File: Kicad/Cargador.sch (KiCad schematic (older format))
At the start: 7 parts, among them P3 USB_A, U4 MCP73831

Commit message: Agregados footprints de pin headers para elementos faltantes (falta USB)
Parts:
- D1: footprint (none) -> EMG:Pin_Header_Straight_1x02_Pitch2.54mm
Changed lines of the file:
@@
 F 0 "D1" H 4150 3450 50  0000 C CNN
 F 1 "LED" H 4150 3250 50  0000 C CNN
-F 2 "" H 4150 3350 50  0001 C CNN
+F 2 "EMG:Pin_Header_Straight_1x02_Pitch2.54mm" H 4150 3350 50  0001 C CNN
 F 3 "" H 4150 3350 50  0000 C CNN
 	1    4150 3350
@@
 	5700 3250 6000 3250
 $Comp
-L +BATT #PWR25
+L +BATT #PWR023
 U 1 1 57E062FB
 P 6400 3100
-F 0 "#PWR25" H 6400 2950 50  0001 C CNN
+F 0 "#PWR023" H 6400 2950 50  0001 C CNN
 F 1 "+BATT" H 6400 3240 50  0000 C CNN
 F 2 "" H 6400 3100 50  0000 C CNN
@@
 Connection ~ 3900 3100
 $Comp
-L GND #PWR23
+L GND #PWR024
 U 1 1 57FAD4CF
 P 3900 3400
-F 0 "#PWR23" H 3900 3150 50  0001 C CNN
+F 0 "#PWR024" H 3900 3150 50  0001 C CNN
 F 1 "GND" H 3900 3250 50  0000 C CNN
 F 2 "" H 3900 3400 50  0000 C CNN
@@
 $EndComp
 $Comp
-L GND #PWR24
+L GND #PWR025
 U 1 1 57FAD4F1
 P 6000 3550
-F 0 "#PWR24" H 6000 3300 50  0001 C CNN
+F 0 "#PWR025" H 6000 3300 50  0001 C CNN
 F 1 "GND" H 6000 3400 50  0000 C CNN
 F 2 "" H 6000 3550 50  0000 C CNN

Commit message: Footprint del conector micro-usb vertical realizado.
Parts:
- P3: footprint (none) -> EMG:usb_vert
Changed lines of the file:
@@
 F 0 "P3" H 3300 3100 50  0000 C CNN
 F 1 "USB_A" H 3050 3500 50  0000 C CNN
-F 2 "" V 3050 3200 50  0001 C CNN
+F 2 "EMG:usb_vert" V 3050 3200 50  0001 C CNN
 F 3 "" V 3050 3200 50  0000 C CNN
 	1    3100 3300

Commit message: Se inició con el Pcb. Se eliminó el capacitor del socket del nrf. Se cambió el conector de la bat.
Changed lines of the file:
@@
 	4300 3550 4150 3550
 Wire Wire Line
-	4150 3150 4150 3100
+	4150 3100 4150 3150
 Wire Wire Line
 	3400 3100 4750 3100

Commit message: Versión unificada
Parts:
- C7, C8: footprint EMG:C_0805 -> EMG:C_0603
- R21, R22: footprint EMG:R_0805 -> EMG:R_0603
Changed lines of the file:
@@
 F 0 "C8" H 6425 3450 50  0000 L CNN
 F 1 "CP" H 6425 3250 50  0000 L CNN
-F 2 "EMG:C_0805" H 6438 3200 50  0001 C CNN
+F 2 "EMG:C_0603" H 6438 3200 50  0001 C CNN
 F 3 "" H 6400 3350 50  0000 C CNN
 	1    6400 3350
@@
 F 0 "C7" H 3925 3350 50  0000 L CNN
 F 1 "CP" H 3925 3150 50  0000 L CNN
-F 2 "EMG:C_0805" H 3938 3100 50  0001 C CNN
+F 2 "EMG:C_0603" H 3938 3100 50  0001 C CNN
 F 3 "" H 3900 3250 50  0000 C CNN
 	1    3900 3250
@@
 F 0 "R22" V 6080 3400 50  0000 C CNN
 F 1 "R" V 6000 3400 50  0000 C CNN
-F 2 "EMG:R_0805" V 5930 3400 50  0001 C CNN
+F 2 "EMG:R_0603" V 5930 3400 50  0001 C CNN
 F 3 "" H 6000 3400 50  0000 C CNN
 	1    6000 3400
@@
 F 0 "R21" V 4530 3550 50  0000 C CNN
 F 1 "R" V 4450 3550 50  0000 C CNN
-F 2 "EMG:R_0805" V 4380 3550 50  0001 C CNN
+F 2 "EMG:R_0603" V 4380 3550 50  0001 C CNN
 F 3 "" H 4450 3550 50  0000 C CNN
 	1    4450 3550

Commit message: Cambios en tamaño de pinheaders
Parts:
- D1: footprint EMG:Pin_Header_Straight_1x02_Pitch2.54mm -> EMG:Pin_Header_Straight_1x02_Pitch1.27mm
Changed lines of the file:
@@
 F 0 "D1" H 4150 3450 50  0000 C CNN
 F 1 "LED" H 4150 3250 50  0000 C CNN
-F 2 "EMG:Pin_Header_Straight_1x02_Pitch2.54mm" H 4150 3350 50  0001 C CNN
+F 2 "EMG:Pin_Header_Straight_1x02_Pitch1.27mm" H 4150 3350 50  0001 C CNN
 F 3 "" H 4150 3350 50  0000 C CNN
 	1    4150 3350

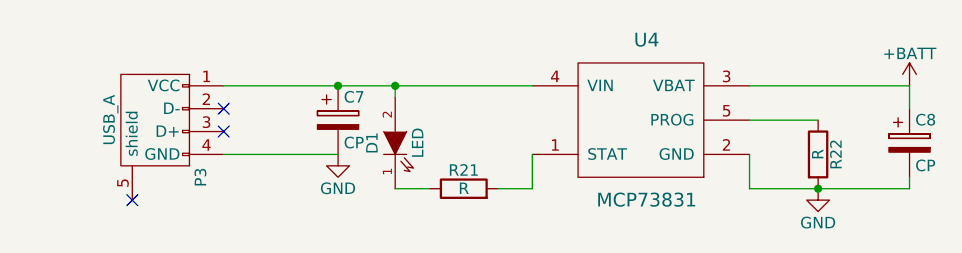
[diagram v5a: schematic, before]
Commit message: Cambiado el switch por uno de punto medio. Aumento de ancho en pistas de alimentación. Plano de masa
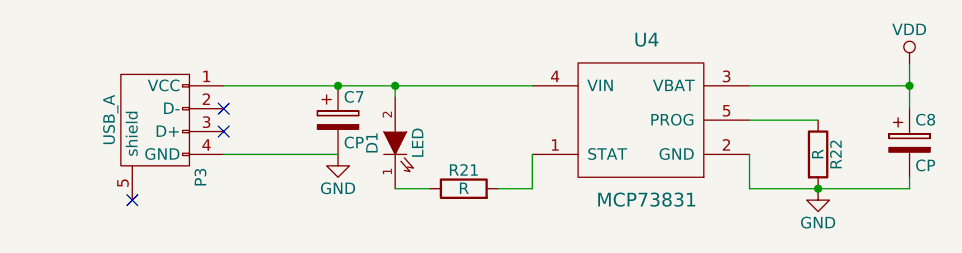
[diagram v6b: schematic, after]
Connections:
- net +BATT renamed VDD
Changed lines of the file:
@@
 	5700 3250 6000 3250
-$Comp
-L +BATT #PWR023
-U 1 1 57E062FB
-P 6400 3100
-F 0 "#PWR023" H 6400 2950 50  0001 C CNN
-F 1 "+BATT" H 6400 3240 50  0000 C CNN
-F 2 "" H 6400 3100 50  0000 C CNN
-F 3 "" H 6400 3100 50  0000 C CNN
-	1    6400 3100
-	1    0    0    -1
-$EndComp
 $Comp
 L USB_A P3
@@
 	5700 3100 6400 3100
 Wire Wire Line
-	6400 3100 6400 3200
+	6400 3005 6400 3200
 NoConn ~ 3400 3200
 NoConn ~ 3400 3300
 NoConn ~ 3000 3600
+$Comp
+L VDD #PWR026
+U 1 1 58DE8D14
+P 6400 3005
+F 0 "#PWR026" H 6400 2855 50  0001 C CNN
+F 1 "VDD" H 6400 3155 50  0000 C CNN
+F 2 "" H 6400 3005 50  0000 C CNN
+F 3 "" H 6400 3005 50  0000 C CNN
+	1    6400 3005
+	1    0    0    -1
+$EndComp
+Connection ~ 6400 3100
 $EndSCHEMATC

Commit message: Se creó el footprint usb_vert_2, y se cambió el pin out del usb en el esquema
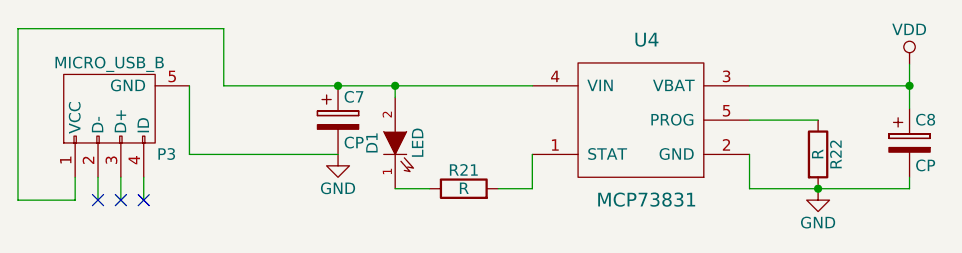
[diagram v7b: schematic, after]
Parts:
- removed P3: USB_A, EMG:usb_vert, symbol USB_A
- added P3: MICRO_USB_B, symbol MICRO_USB_B
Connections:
- net GND: now also P3.5 (GND)
- net at C7.1, D1.2 (A), U4.4 (VIN): now also P3.1 (VCC)
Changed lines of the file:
@@
 Wire Wire Line
 	5700 3250 6000 3250
-$Comp
-L USB_A P3
-U 1 1 57E06354
-P 3100 3300
-F 0 "P3" H 3300 3100 50  0000 C CNN
-F 1 "USB_A" H 3050 3500 50  0000 C CNN
-F 2 "EMG:usb_vert" V 3050 3200 50  0001 C CNN
-F 3 "" V 3050 3200 50  0000 C CNN
-	1    3100 3300
-	0    -1   1    0
-$EndComp
 Connection ~ 3900 3100
 $Comp
-L GND #PWR024
+L GND #PWR24
 U 1 1 57FAD4CF
 P 3900 3400
-F 0 "#PWR024" H 3900 3150 50  0001 C CNN
+F 0 "#PWR24" H 3900 3150 50  0001 C CNN
 F 1 "GND" H 3900 3250 50  0000 C CNN
 F 2 "" H 3900 3400 50  0000 C CNN
@@
 $EndComp
 $Comp
-L GND #PWR025
+L GND #PWR25
 U 1 1 57FAD4F1
 P 6000 3550
-F 0 "#PWR025" H 6000 3300 50  0001 C CNN
+F 0 "#PWR25" H 6000 3300 50  0001 C CNN
 F 1 "GND" H 6000 3400 50  0000 C CNN
 F 2 "" H 6000 3550 50  0000 C CNN
@@
 $EndComp
 Wire Wire Line
-	3400 3400 3900 3400
+	3250 3400 3900 3400
 Wire Wire Line
 	5700 3400 5700 3550
@@
 Wire Wire Line
 	6400 3005 6400 3200
-NoConn ~ 3400 3200
-NoConn ~ 3400 3300
-NoConn ~ 3000 3600
+NoConn ~ 2850 3600
+NoConn ~ 3050 3600
+NoConn ~ 2950 3600
 $Comp
-L VDD #PWR026
+L VDD #PWR26
 U 1 1 58DE8D14
 P 6400 3005
-F 0 "#PWR026" H 6400 2855 50  0001 C CNN
+F 0 "#PWR26" H 6400 2855 50  0001 C CNN
 F 1 "VDD" H 6400 3155 50  0000 C CNN
 F 2 "" H 6400 3005 50  0000 C CNN
@@
 $EndComp
 Connection ~ 6400 3100
+$Comp
+L MICRO_USB_B P3
+U 1 1 58DEA833
+P 2950 3200
+F 0 "P3" H 3150 3000 50  0000 C CNN
+F 1 "MICRO_USB_B" H 2900 3400 50  0000 C CNN
+F 2 "" V 2900 3100 50  0000 C CNN
+F 3 "" V 2900 3100 50  0000 C CNN
+	1    2950 3200
+	1    0    0    -1
+$EndComp
+Wire Wire Line
+	2750 3500 2750 3600
+Wire Wire Line
+	2750 3600 2500 3600
+Wire Wire Line
+	2500 3600 2500 2850
+Wire Wire Line
+	2500 2850 3400 2850
+Wire Wire Line
+	3400 2850 3400 3100
+Wire Wire Line
+	3250 3100 3250 3400
+Wire Wire Line
+	3050 3600 3050 3500
+Wire Wire Line
+	2950 3600 2950 3500
+Wire Wire Line
+	2850 3600 2850 3500
 $EndSCHEMATC

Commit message: Se cambió el footprint del usb.
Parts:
- P3: footprint (none) -> EMG:usb_vert_2
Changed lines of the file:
@@
 Connection ~ 3900 3100
 $Comp
-L GND #PWR24
+L GND #PWR024
 U 1 1 57FAD4CF
 P 3900 3400
-F 0 "#PWR24" H 3900 3150 50  0001 C CNN
+F 0 "#PWR024" H 3900 3150 50  0001 C CNN
 F 1 "GND" H 3900 3250 50  0000 C CNN
 F 2 "" H 3900 3400 50  0000 C CNN
@@
 $EndComp
 $Comp
-L GND #PWR25
+L GND #PWR025
 U 1 1 57FAD4F1
 P 6000 3550
-F 0 "#PWR25" H 6000 3300 50  0001 C CNN
+F 0 "#PWR025" H 6000 3300 50  0001 C CNN
 F 1 "GND" H 6000 3400 50  0000 C CNN
 F 2 "" H 6000 3550 50  0000 C CNN
@@
 NoConn ~ 2950 3600
 $Comp
-L VDD #PWR26
+L VDD #PWR026
 U 1 1 58DE8D14
 P 6400 3005
-F 0 "#PWR26" H 6400 2855 50  0001 C CNN
+F 0 "#PWR026" H 6400 2855 50  0001 C CNN
 F 1 "VDD" H 6400 3155 50  0000 C CNN
 F 2 "" H 6400 3005 50  0000 C CNN
@@
 F 0 "P3" H 3150 3000 50  0000 C CNN
 F 1 "MICRO_USB_B" H 2900 3400 50  0000 C CNN
-F 2 "" V 2900 3100 50  0000 C CNN
+F 2 "EMG:usb_vert_2" V 2900 3100 50  0001 C CNN
 F 3 "" V 2900 3100 50  0000 C CNN
 	1    2950 3200
